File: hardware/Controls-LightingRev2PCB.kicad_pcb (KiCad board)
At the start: 2 copper layers, 50.2 x 53.5 mm, 54 parts, among them IC1 LM74502HDDFR, IC2 TLV70433DBVT, IC3 TLV70130DBVR, J2 MX150_02x08_RightAngle, J3 53307-2471, Q2 IRLML0030, Q3 IRLML0030, Q4 PSMN8R5-40MSDX, U1 TLV2371DBV, U2 INA241A5xD, U3 INA241A5xD, U4 INA241A5xD, U5 SN74LV1T34DBV, U8 TLV2371DBV, U9 TLV2371DBV

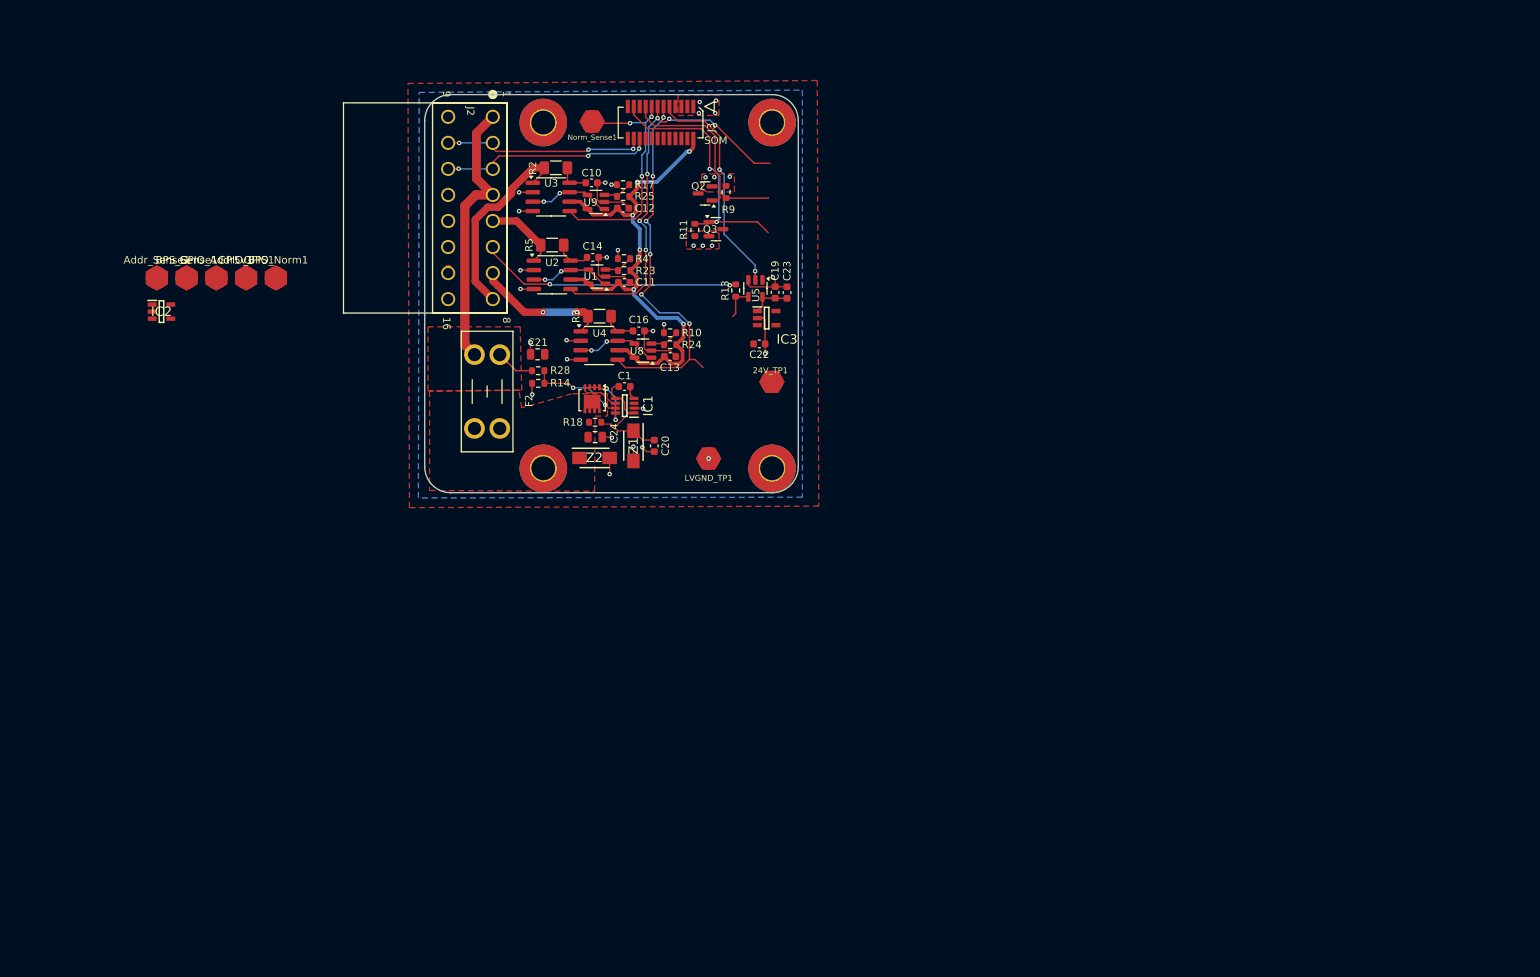
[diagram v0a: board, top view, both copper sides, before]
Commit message: Switched MX150 to 02x05 nanofet
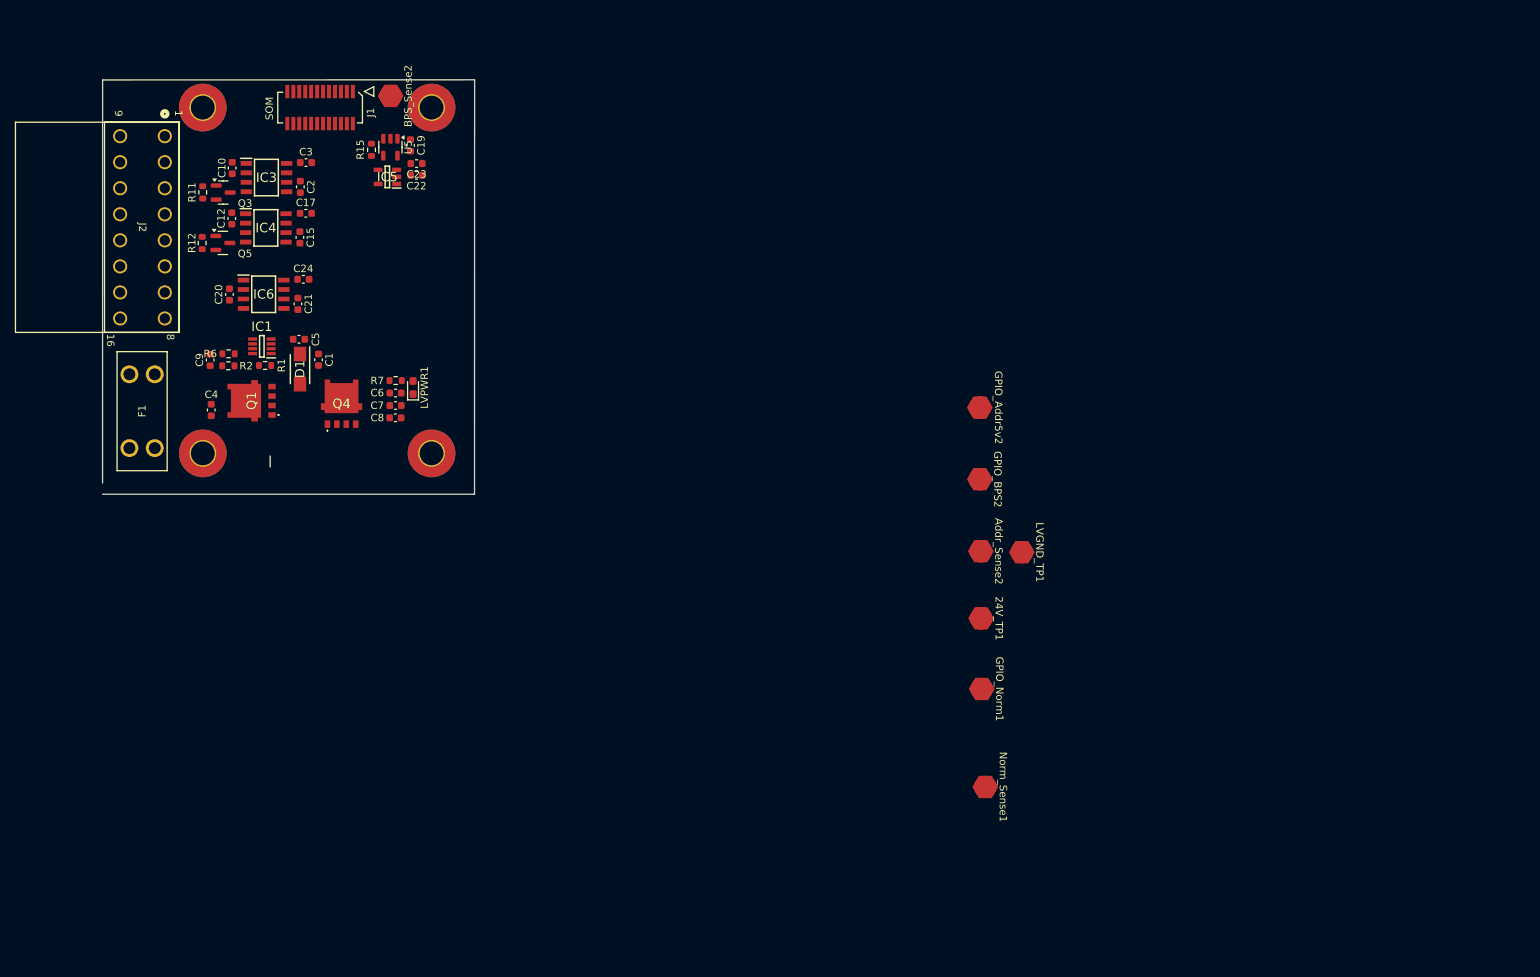
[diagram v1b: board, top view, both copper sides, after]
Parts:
- removed Addr_Sense1, BPS_Sense1, GPIO_Addr5v1, GPIO_BPS1: TestPoint, UTSVT_Special:TestPoint_HEX_3mmID
- removed C11, C13, C14, C16: 0.1uF, Capacitor_SMD:C_0603_1608Metric
- removed F2: 4A, Fuse:Fuseholder_Blade_Mini_Keystone_3568
- removed IC2: TLV70433DBVT, Lighting_Board:SOT95P280X145-5N
- removed J3: 53307-2471, UTSVT_Connectors:PeripheralSOM
- removed Q2: IRLML0030, Package_TO_SOT_SMD:SOT-23
- removed R10, R17, R4: 3.3k, Resistor_SMD:R_0603_1608Metric
- removed R13, R23, R24, R25: 100k, Resistor_SMD:R_0603_1608Metric
- removed R14: 9k, Resistor_SMD:R_0603_1608Metric
- removed R18, R9: 10k, Resistor_SMD:R_0603_1608Metric
- removed R28: 200k, Resistor_SMD:R_0603_1608Metric
- removed R3: 90m, Resistor_SMD:R_1206_3216Metric_Pad1.30x1.75mm_HandSolder
- removed R5: 12m, Resistor_SMD:R_1206_3216Metric_Pad1.30x1.75mm_HandSolder
- removed U1, U8, U9: TLV2371DBV, Package_TO_SOT_SMD:SOT-23-5
- removed U2, U3, U4: INA241A5xD, Package_SO:SOIC-8_3.9x4.9mm_P1.27mm
- removed Z1, Z2: SMAF4751A-TP, UTSVT_Passive:SODFL5026X125N
- added Addr_Sense2: TestPoint, UTSVT_Special:TestPoint_HEX_3mmID, F.Cu at (155.4, 83.3)
- added BPS_Sense2: TestPoint, UTSVT_Special:TestPoint_HEX_3mmID, F.Cu at (76.1, 22.1)
- added C15: 1nF, Capacitor_SMD:C_0603_1608Metric, F.Cu at (63.9, 41.1)
- added C17: 0.1uF, Capacitor_SMD:C_0603_1608Metric, F.Cu at (64.7, 37.8)
- added C2: 1nf, Capacitor_SMD:C_0603_1608Metric, F.Cu at (63.9, 34.3)
- added C3: 0.1uf, Capacitor_SMD:C_0603_1608Metric, F.Cu at (64.7, 31.0)
- added C4: 0.1uF, Capacitor_SMD:C_0603_1608Metric, F.Cu at (52.0, 64.3)
- added C5: 220nF, Capacitor_SMD:C_0603_1608Metric, F.Cu at (63.8, 54.8)
- added C6: 10uF, Capacitor_SMD:C_0603_1608Metric, F.Cu at (76.7, 62.0)
- added C7: 10u, Capacitor_SMD:C_0603_1608Metric, F.Cu at (76.7, 63.7)
- added C8: 0.1u, Capacitor_SMD:C_0603_1608Metric, F.Cu at (76.7, 65.3)
- added C9: 1u, Capacitor_SMD:C_0603_1608Metric, F.Cu at (51.8, 57.6)
- added D1: SMAF4758A, UTSVT_Passive:SODFL5026X125N, F.Cu at (63.9, 58.8)
- added F1: 4A, UTSVT_Connectors:FUSE_3568, F.Cu at (42.7, 64.4)
- added GPIO_Addr5v2: TestPoint, UTSVT_Special:TestPoint_HEX_3mmID, F.Cu at (155.2, 64.0)
- added GPIO_BPS2: TestPoint, UTSVT_Special:TestPoint_HEX_3mmID, F.Cu at (155.2, 73.6)
- added IC4: ACS724LLCTR-05AU-T, Lighting_IC:SOIC127P600X175-8N, F.Cu at (59.3, 39.8)
- added IC5: TLV70433DBVT, Lighting_Board:SOT95P280X145-5N, F.Cu at (75.6, 33.0)
- added IC6: ACS724LLCTR-05AU-T, Lighting_IC:SOIC127P600X175-8N, F.Cu at (59.0, 48.7)
- added J1: 53307-2471, UTSVT_Connectors:PeripheralSOM, F.Cu at (66.6, 23.6)
- added LVPWR1: LED, LED_SMD:LED_0603_1608Metric_Pad1.05x0.95mm_HandSolder, F.Cu at (79.1, 61.3)
- added Q1: NVMFWS1D7N04XMT1G, UTSVT_Power:NVMFWS3D0P04M8LT1G, F.Cu at (57.4, 63.0)
- added Q5: IRLML0030, Package_TO_SOT_SMD:SOT-23, F.Cu at (53.5, 41.8)
- added R1: 10k, Resistor_SMD:R_0603_1608Metric, F.Cu at (59.2, 58.3)
- added R12: 10k, Resistor_SMD:R_0603_1608Metric, F.Cu at (50.7, 41.8)
- added R15: 100k, Resistor_SMD:R_0603_1608Metric, F.Cu at (73.5, 29.3)
- added R6: 9k, Resistor_SMD:R_0603_1608Metric, F.Cu at (54.3, 56.7)
- added R7: 4.3k, Resistor_SMD:R_0603_1608Metric, F.Cu at (76.7, 60.3)
- C1: value 220n -> 1uF
- C20: value 1uF -> 0.1uF
- C21: value 220u -> 1nF; footprint Capacitor_SMD:C_0805_2012Metric -> Capacitor_SMD:C_0603_1608Metric
- C24: value 220u -> 0.1uF; footprint Capacitor_SMD:C_0805_2012Metric -> Capacitor_SMD:C_0603_1608Metric
- IC3: value TLV70130DBVR -> ACS724LLCTR-05AU-T; footprint UTSVT_Power:TLV70130DBVR -> Lighting_IC:SOIC127P600X175-8N
- Q4: value PSMN8R5-40MSDX -> NVMFWS1D7N04XMT1G; footprint UTSVT_Power:PSMN8R5-40MSDX -> UTSVT_Power:NVMFWS3D0P04M8LT1G
- R2: value 12m -> 200k; footprint Resistor_SMD:R_1206_3216Metric_Pad1.30x1.75mm_HandSolder -> Resistor_SMD:R_0603_1608Metric
- moved GPIO_Norm1 109.8 mm to (155.5, 101.8), turned to -90 degrees
- moved Norm_Sense1 103.9 mm to (156.0, 114.9), turned to -90 degrees
- moved IC3 69.8 mm to (59.4, 33.0)
- moved Q3 66.4 mm to (53.6, 35.1)
- moved R11 66.3 mm to (50.8, 35.0)
- moved C20 60.6 mm to (54.4, 48.8)
- moved C19 52.8 mm to (78.7, 28.7)
- moved C23 52.7 mm to (79.6, 31.2), turned to 180 degrees
- moved C12 52.6 mm to (54.7, 38.5), turned to -90 degrees
- moved U5 52.6 mm to (76.0, 29.0)
- moved R2 51.4 mm to (54.3, 58.3), turned to 0 degrees
- moved C22 51.3 mm to (79.5, 32.7)
- moved IC1 49.4 mm to (58.8, 55.7)
- moved C10 48.3 mm to (54.8, 31.8), turned to -90 degrees
- moved C24 44.6 mm to (64.3, 46.7)
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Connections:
- 24V_TP1 pad 1: +24V -> Addressable_PWR
- C1 pad 1: /Reverse Polarity Protection/RPP_EN -> Addressable_GND
- C1 pad 2: Net-(IC1-VCAP) -> /Reverse Polarity Protection/RPP_EN
- C10 pad 2: +24V -> Addressable_PWR
- C12 pad 2: +3.3V -> Addressable_PWR
- C20 pad 2: /Reverse Polarity Protection/RPP_EN -> Addressable_PWR
- C21 pad 1: +24V -> Net-(IC6-FILTER)
- C22 pad 2: +24V -> Addressable_PWR
- C24 pad 1: Net-(Q4-D) -> 5V PWR
- IC1 pad 8: +24V -> Net-(IC1-SRC)
- IC3 pad 1: unconnected-(IC3-OUT-Pad1) -> Addressable_PWR
- IC3 pad 2: unconnected-(IC3-GND-Pad2) -> Addressable_PWR
- IC3 pad 3: unconnected-(IC3-IN-Pad3) -> Normal_GND
- IC3 pad 4: unconnected-(IC3-NC_1-Pad4) -> Normal_GND
- IC3 pad 5: unconnected-(IC3-NC_2-Pad5) -> Addressable_GND
- J2 pad 1: 24V_Ext -> 24V_EXT
- J2 pad 15: Strobe_GND -> Normal_GND
- J2 pad 16: Normal_GND -> Strobe_GND
- J2 pad 4: 24V_Ext -> 24V_EXT
- J2 pad 7: Strobe_PWR -> Addressable_PWR
- J2 pad 8: Normal_PWR -> Addressable_PWR
- Q4 pad 1: +24V -> Net-(IC1-SRC)
- Q4 pad 2: Net-(IC1-GATE) -> Net-(IC1-SRC)
- Q4 pad 3: Net-(Q4-D) -> Net-(IC1-SRC)
- R2 pad 1: +24V -> 24V_EXT
- R2 pad 2: Normal_PWR -> Net-(IC1-OV)
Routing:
- net +3.3V: track 72.3 -> 0.00 mm, vias 6 -> 0
- net Addressable_GND: track 63.2 -> 0.00 mm, vias 32 -> 0
- net ADDR_Sense: track 54.5 -> 0.00 mm, vias 6 -> 0
- net BPS_Sense: track 52.7 -> 0.00 mm, vias 6 -> 0
- net 24V_Ext: track 42.5 -> 0.00 mm
- net GPIO_Normal: track 35.5 -> 0.00 mm, vias 2 -> 0
- net Addressable_Logic: track 35.3 -> 0.00 mm, vias 2 -> 0
- net NORMAL_Sense: track 32.6 -> 0.00 mm, vias 3 -> 0
- net GPIO_Addr: track 30.3 -> 0.00 mm, vias 2 -> 0
- net GPIO_BPS_Strobe: track 28.9 -> 0.00 mm
- net CAN_L: track 28.8 -> 0.00 mm, vias 3 -> 0
- net CAN_H: track 27.4 -> 0.00 mm, vias 3 -> 0
- net Normal_PWR: track 26.8 -> 0.00 mm
- net +24V: track 21.7 -> 0.00 mm, vias 2 -> 0
- net Strobe_PWR: track 18.3 -> 0.00 mm, vias 2 -> 0
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- removed copper zone on F.Cu, net +24V
- removed copper zone on F.Cu, net 24V_Ext
- removed copper zone on B.Cu, net Addressable_GND
- removed copper zone on F.Cu, net Addressable_GND
- removed copper zone on F.Cu, net Net-(Q4-D)
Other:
- board size 50.2 x 53.5 mm -> 50 x 55.7 mm

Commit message: Current Layout
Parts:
- removed J2: MX150_02x08_RightAngle, UTSVT_Connectors:MX150_02x08_RightAngle
- added J3: Conn_02x05_Top_Bottom, Connector_Molex:Molex_Nano-Fit_105314-xx10_2x05_P2.50mm_Horizontal, F.Cu at (50.9, 39.8)
- added J4: Conn_01x02, UTSVT_Connectors:105313-2102, F.Cu at (74.5, 38.1)
- added J5: Conn_01x02, UTSVT_Connectors:105313-2102, F.Cu at (74.7, 30.2)
- added J6: Conn_01x03, UTSVT_Connectors:105313-1103, F.Cu at (68.8, 84.0)
- moved C19 63.4 mm to (58.6, 88.8), turned to 90 degrees
- moved U5 61.4 mm to (61.3, 88.6), turned to 90 degrees
- moved Norm_Sense1 59.9 mm to (132.0, 60.0), turned to 0 degrees
- moved R15 59.7 mm to (63.9, 88.3), turned to 90 degrees
- moved C23 59.4 mm to (57.8, 86.4), turned to 0 degrees
- moved C22 56.4 mm to (57.8, 84.8), turned to 0 degrees
- moved BPS_Sense2 55.1 mm to (116.0, 60.0), turned to 0 degrees
- moved IC5 53.5 mm to (61.7, 84.6), turned to 0 degrees
- moved 24V_TP1 50.5 mm to (112.0, 66.5), turned to 0 degrees
- moved GPIO_Norm1 50.0 mm to (128.0, 60.0), turned to 0 degrees
- moved Addr_Sense2 49.2 mm to (112.0, 60.0), turned to 0 degrees
- moved LVGND_TP1 48.0 mm to (116.0, 66.5), turned to 0 degrees
- moved GPIO_Addr5v2 35.5 mm to (120.0, 60.0), turned to 0 degrees
- moved GPIO_BPS2 34.1 mm to (124.0, 60.0), turned to 0 degrees
- moved F1 13.6 mm to (41.9, 50.9)
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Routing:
- net Addressable_GND: vias 0 -> 1
- added copper zone on B.Cu, net Addressable_GND
- added copper zone on F.Cu, net Addressable_PWR
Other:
- board size 50 x 55.7 mm -> 50 x 53.5 mm

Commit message: Layout
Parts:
- moved C22 57.4 mm to (77.2, 30.8)
- moved U5 57.4 mm to (80.7, 34.6)
- moved C19 57.4 mm to (78.0, 34.8)
- moved C23 57.4 mm to (77.2, 32.4)
- moved R15 57.4 mm to (83.2, 34.2)
- moved IC5 57.4 mm to (81.1, 30.6)
- moved J6 57.4 mm to (88.7, 30.2)
- moved J5 21.5 mm to (88.7, 46.6)
- moved J4 21.2 mm to (88.7, 53.8)
- moved C10 19.8 mm to (73.3, 46.4)
- moved C15 19.8 mm to (82.5, 56.4)
- moved C17 19.8 mm to (83.3, 53.2)
- moved C2 19.8 mm to (82.4, 49.0)
- moved C3 19.8 mm to (83.2, 45.7)
- moved IC4 19.8 mm to (77.9, 55.2)
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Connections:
- J1 pad 11: BPS_Sense -> ADDR_Sense
- J1 pad 13: ADDR_Sense -> NORMAL_Sense
- J1 pad 15: NORMAL_Sense -> BPS_Sense
- J1 pad 17: GPIO_BPS_Strobe -> GPIO_Normal
- J1 pad 21: GPIO_Normal -> GPIO_BPS_Strobe
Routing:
- net Addressable_GND: vias 1 -> 0
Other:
- board size 50 x 53.5 mm -> 68 x 56 mm

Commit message: Layout 53.5
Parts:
- moved J3 49.8 mm to (88.4, 15.1), turned to 0 degrees
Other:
- board size 68 x 56 mm -> 53.5 x 53.5 mm

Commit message: layout recommendations
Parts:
- moved C23 172.8 mm to (219.8, 130.0), turned to 90 degrees
- moved C22 172.4 mm to (218.3, 130.0), turned to 90 degrees
- moved C19 172.4 mm to (222.3, 129.2), turned to 180 degrees
- moved U5 168.6 mm to (222.0, 126.5), turned to 180 degrees
- moved IC5 166.9 mm to (218.0, 126.0), turned to 90 degrees
- moved R15 165.0 mm to (221.7, 123.9), turned to 180 degrees
- moved C20 164.5 mm to (212.5, 128.0), turned to -90 degrees
- moved R11 162.6 mm to (216.5, 118.7), turned to -90 degrees
- moved C10 158.4 mm to (212.5, 122.0), turned to 90 degrees
- moved Q3 157.6 mm to (213.7, 118.7), turned to 180 degrees
- moved IC6 156.8 mm to (207.9, 128.0), turned to 180 degrees
- moved J1 156.1 mm to (210.0, 88.5)
- moved C24 150.5 mm to (202.6, 130.0), turned to 180 degrees
- moved IC3 149.1 mm to (207.9, 120.7), turned to 180 degrees
- moved C21 147.8 mm to (203.3, 126.7), turned to 90 degrees
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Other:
- board size 53.5 x 53.5 mm -> 54.5 x 53.5 mm
